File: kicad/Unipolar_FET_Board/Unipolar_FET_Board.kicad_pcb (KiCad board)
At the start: 2 copper layers, 200 x 127 mm, 20 parts, among them J1 Screw_Terminal_01x04, J3 SENSE, J4 N-MOS, Q1 Q_NMOS_GDS, Q2 Q_NMOS_GDS

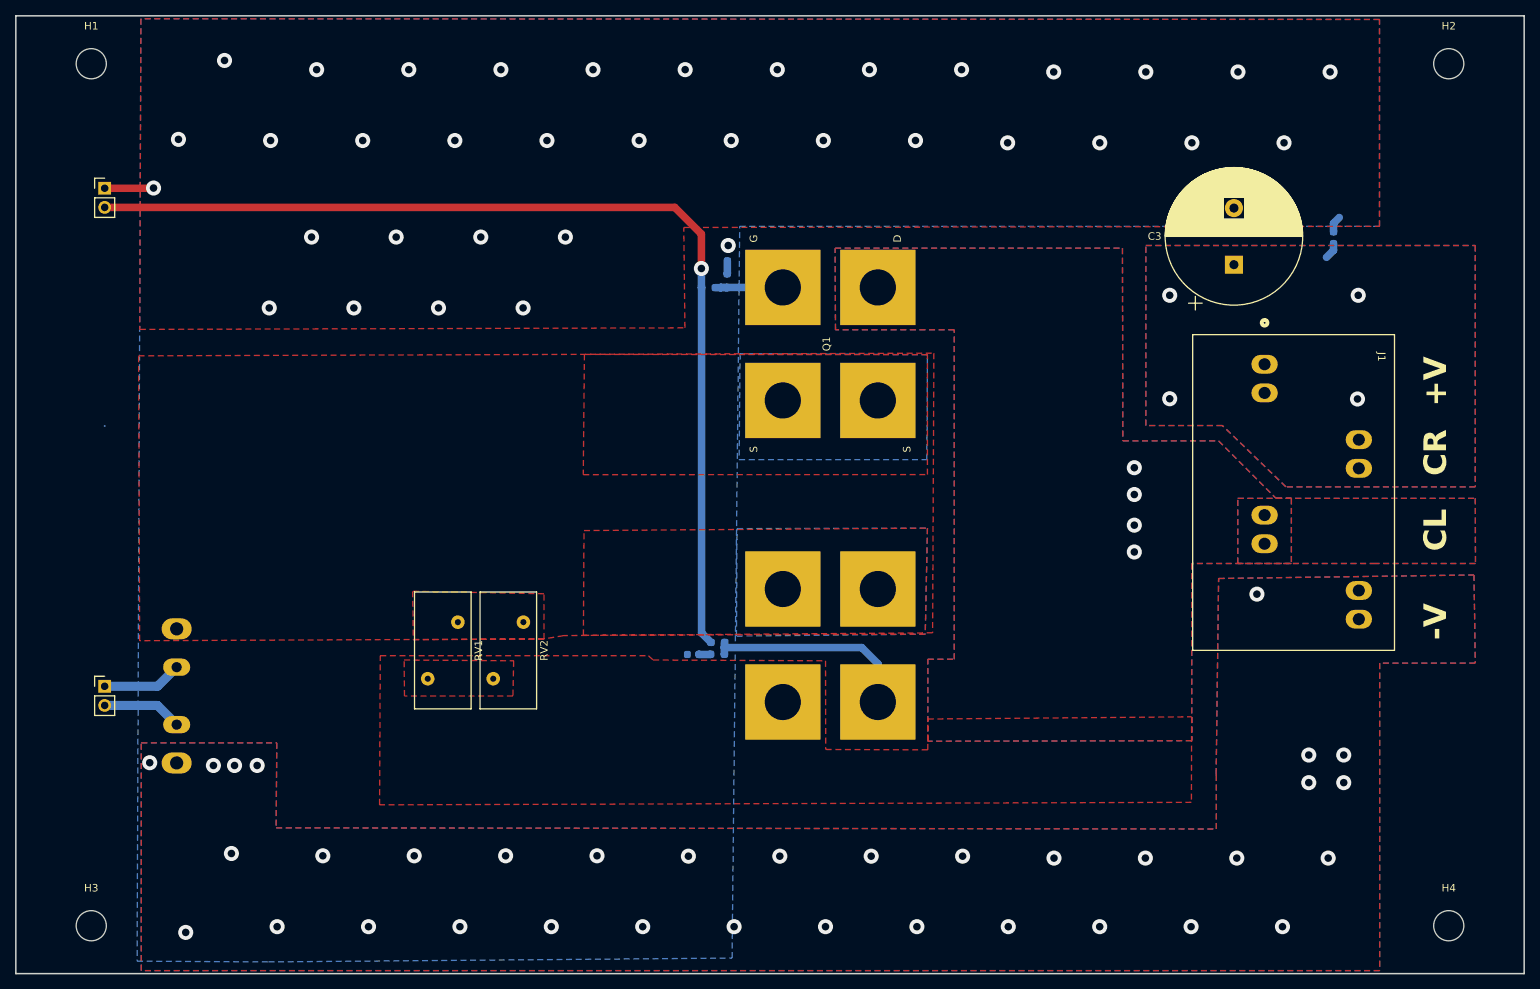
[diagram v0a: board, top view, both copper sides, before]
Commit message: Final Board schematics and layouts, Also added custom footprints that were made for the relay and terminal connector block.
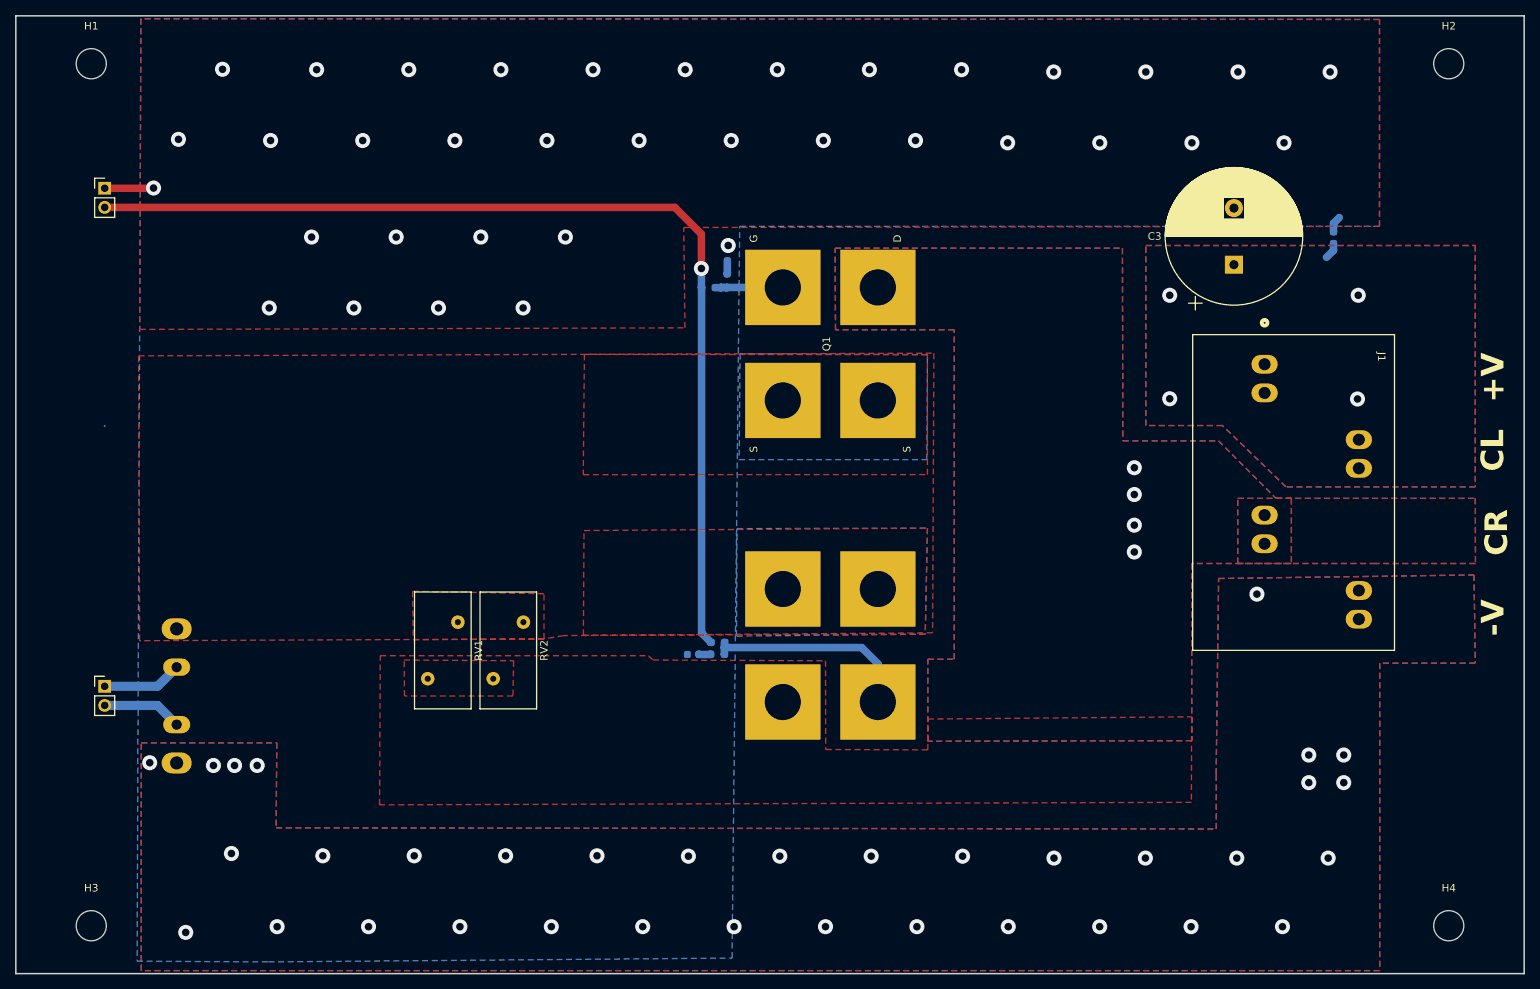
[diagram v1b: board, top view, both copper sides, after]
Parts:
- C1: value 0.1uF -> 1.1uF
- C2, C5: value 0.1uF -> 2.2uF
- R1, R2: value 20 -> 330
- R3, R4: value 20 -> 33
- R9: value R_Shunt -> 0.01 R_Shunt
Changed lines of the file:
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@@
 			)
 		)
-		(property "Value" "R_Shunt"
+		(property "Value" "0.01 R_Shunt"
 			(at -0.1 3 -90)
 			(unlocked yes)
@@
 			)
 		)
+		(property "DIGIKEY" "696-PCS-0R01D1-ND"
+			(at 0 0 -90)
+			(unlocked yes)
+			(layer "F.Fab")
+			(hide yes)
+			(effects
+				(font
+					(size 1 1)
+					(thickness 0.15)
+				)
+			)
+		)
+		(property "PARTNO" "PCS-0R01D1"
+			(at 0 0 -90)
+			(unlocked yes)
+			(layer "F.Fab")
+			(hide yes)
+			(effects
+				(font
+					(size 1 1)
+					(thickness 0.15)
+				)
+			)
+		)
 		(property ki_fp_filters "R_*Shunt*")
 		(sheetname "Root")
@@
 			)
 		)
-		(property "DIGIKEY" ""
+		(property "DIGIKEY" "2453710000-ND"
 			(at 0 0 -90)
 			(unlocked yes)
@@
 			)
 		)
-		(property "PARTNO" ""
+		(property "PARTNO" "2453710000"
 			(at 0 0 -90)
 			(unlocked yes)
@@
 			)
 		)
-		(property "DIGIKEY PARTNO" "IXFN520N075T2-ND"
-			(at 211.505 -64.495 0)
+		(property "DIGIKEY" "IXFN520N075T2-ND"
+			(at 0 0 90)
+			(unlocked yes)
+			(layer "B.Fab")
+			(hide yes)
+			(effects
+				(font
+					(size 1 1)
+					(thickness 0.15)
+				)
+				(justify mirror)
+			)
+		)
+		(property "PARTNO" "IXFN520N075T2"
+			(at 0 0 90)
+			(unlocked yes)
 			(layer "B.Fab")
 			(hide yes)
@@
 			)
 		)
-		(property "Value" "0.1uF"
+		(property "Value" "2.2uF"
 			(at 0 -1.43 0)
 			(layer "B.Fab")
@@
 			)
 		)
+		(property "DIGIKEY" "311-1140-1-ND"
+			(at 0 0 0)
+			(unlocked yes)
+			(layer "B.Fab")
+			(hide yes)
+			(effects
+				(font
+					(size 1 1)
+					(thickness 0.15)
+				)
+				(justify mirror)
+			)
+		)
+		(property "PARTNO" "CC0805KRX7R9BB104"
+			(at 0 0 0)
+			(unlocked yes)
+			(layer "B.Fab")
+			(hide yes)
+			(effects
+				(font
+					(size 1 1)
+					(thickness 0.15)
+				)
+				(justify mirror)
+			)
+		)
 		(property ki_fp_filters "C_*")
 		(sheetname "Root")
@@
 			)
 		)
-		(property "Value" "0.1uF"
+		(property "Value" "1.1uF"
 			(at 0 -1.43 90)
 			(layer "B.Fab")
@@
 			)
 		)
+		(property "DIGIKEY" "311-1140-1-ND"
+			(at 0 0 90)
+			(unlocked yes)
+			(layer "B.Fab")
+			(hide yes)
+			(effects
+				(font
+					(size 1 1)
+					(thickness 0.15)
+				)
+				(justify mirror)
+			)
+		)
+		(property "PARTNO" "CC0805KRX7R9BB104"
+			(at 0 0 90)
+			(unlocked yes)
+			(layer "B.Fab")
+			(hide yes)
+			(effects
+				(font
+					(size 1 1)
+					(thickness 0.15)
+				)
+				(justify mirror)
+			)
+		)
 		(property ki_fp_filters "C_*")
 		(sheetname "Root")
@@
 			)
 		)
-		(property "Value" "0.1uF"
+		(property "Value" "2.2uF"
 			(at 0 -1.43 90)
 			(layer "B.Fab")
@@
 			)
 		)
+		(property "DIGIKEY" "311-1140-1-ND"
+			(at 0 0 -90)
+			(unlocked yes)
+			(layer "B.Fab")
+			(hide yes)
+			(effects
+				(font
+					(size 1 1)
+					(thickness 0.15)
+				)
+				(justify mirror)
+			)
+		)
+		(property "PARTNO" "CC0805KRX7R9BB104"
+			(at 0 0 -90)
+			(unlocked yes)
+			(layer "B.Fab")
+			(hide yes)
+			(effects
+				(font
+					(size 1 1)
+					(thickness 0.15)
+				)
+				(justify mirror)
+			)
+		)
 		(property ki_fp_filters "C_*")
 		(sheetname "Root")
@@
 			)
 		)
-		(property "Value" "20"
+		(property "Value" "330"
 			(at 0 -1.43 0)
 			(layer "B.Fab")
@@
 			)
 		)
-		(property "DIGIKEY PARTNO" "IXFN520N075T2-ND"
-			(at 0 0 90)
+		(property "DIGIKEY" "IXFN520N075T2-ND"
+			(at 0 0 -90)
+			(unlocked yes)
+			(layer "B.Fab")
+			(hide yes)
+			(effects
+				(font
+					(size 1 1)
+					(thickness 0.15)
+				)
+				(justify mirror)
+			)
+		)
+		(property "PARTNO" "IXFN520N075T2"
+			(at 0 0 -90)
 			(unlocked yes)
 			(layer "B.Fab")
@@
 			)
 		)
-		(property "Value" "20"
+		(property "Value" "33"
 			(at 0 -1.43 90)
 			(layer "B.Fab")
@@
 			)
 		)
-		(property "Value" "20"
+		(property "Value" "330"
 			(at 0 -1.43 0)
 			(layer "B.Fab")
@@
 			)
 		)
-		(property "Value" "20"
+		(property "Value" "33"
 			(at 0 -1.43 0)
 			(layer "B.Fab")
@@
 	)
 	(gr_text "+V"
-		(at 220 81.788 90)
+		(at 227.62 81.28 90)
 		(layer "F.SilkS")
 		(effects
@@
 	)
 	(gr_text "CL"
-		(at 220 101 90)
+		(at 227.584 90.424 90)
 		(layer "F.SilkS")
 		(effects
@@
 	)
 	(gr_text "-V"
-		(at 220 112.776 90)
+		(at 227.62 112.268 90)
 		(layer "F.SilkS")
 		(effects
@@
 	)
 	(gr_text "CR"
-		(at 220 91 90)
+		(at 228.092 101.6 90)
 		(layer "F.SilkS")
 		(effects
@@
 	)
 	(via
-		(at 57.670192 35.9156)
+		(at 57.404 37.084)
 		(size 2)
 		(drill 1)
